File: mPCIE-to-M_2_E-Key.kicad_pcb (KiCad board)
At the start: 2 copper layers, 10 parts, among them J2 Bus_M.2_Socket_E, Q1 BSS138K, Q2 BSS138K, U1 TL1963A

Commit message: updated files
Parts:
- added H1: M2.5, lib_fp:M2.5_MH, F.Cu at (145.9, 82.0)
- added H2: M2.5, lib_fp:M2.5_MH, F.Cu at (121.8, 82.0)
- added H3: M3.5, lib_fp:MountingHole_3.5mm_Pad_Via, F.Cu at (133.8, 84.2)
- added J1: Bus_PCI_Express_Mini, lib_fp:BUS_mPCIe, F.Cu at (130.0, 130.0)
- added R5: 100K, lib_fp:CRCW0603, F.Cu at (125.0, 121.8)
- C1: value 10uF -> 100nF; footprint lib_fp:CAPC160X80X88L35N -> lib_fp:MLCC0603
- C2: value 10uF -> 470nF; footprint lib_fp:CAPC160X80X88L35N -> lib_fp:MLCC0805
- R1, R2, R3, R4: footprint lib_fp:RESC160X80X55L30N -> lib_fp:CRCW0603
- U1: value TL1963A -> TPS79718; footprint lib_fp:SOT223-4 -> lib_fp:SOT323-65P210X110-5
- moved C1 43.0 mm to (120.4, 122.8), turned to 90 degrees
- moved C2 35.9 mm to (126.8, 121.7), turned to 90 degrees
- moved Q1 30.2 mm to (129.5, 122.3), turned to 180 degrees
- moved U1 29.2 mm to (122.9, 122.8), turned to 180 degrees
- moved Q2 25.1 mm to (133.1, 122.3), turned to 180 degrees
- moved J2 21.2 mm to (133.8, 112.5), turned to 180 degrees
- moved R1 16.0 mm to (137.2, 123.4), turned to 90 degrees
- moved R3 15.1 mm to (129.5, 119.8), turned to 180 degrees
- moved R2 14.4 mm to (135.8, 123.4), turned to 90 degrees
- moved R4 8.31 mm to (136.5, 120.9)
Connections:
- net Net-(Q1-Pad3) renamed /SCL_3V3
- net Net-(Q2-Pad3) renamed /SDA_3V3
- J2 pad S1: Net-(J2-PadS1) -> GND
- J2 pad S2: Net-(J2-PadS1) -> GND
- Q1 pad 2: Net-(Q1-Pad2) -> /SCL_1V8
- Q2 pad 2: Net-(Q2-Pad2) -> /SDA_1V8
- R3 pad 2: Net-(Q1-Pad2) -> /SCL_1V8
- R4 pad 2: Net-(Q2-Pad2) -> /SDA_1V8
- U1 pad 1: +3V3 -> Net-(U1-PG)
- U1 pad 3: +1V8 -> unconnected-(U1-NC-Pad3)
- U1 pad 4: GND -> +3V3
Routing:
- net +3V3: track 0.00 -> 101.5 mm, vias 0 -> 3
- net GND: track 0.00 -> 66.2 mm, vias 0 -> 77
- net /W_DISABLE: track 0.00 -> 43.7 mm, vias 0 -> 3
- net /SCL_1V8: track 0.00 -> 22.8 mm
- net /SDA_1V8: track 0.00 -> 21.3 mm
- net /SCL_3V3: track 0.00 -> 17.3 mm, vias 0 -> 1
- net +1V8: track 0.00 -> 16.0 mm
- net /D_P: track 0.00 -> 12.2 mm, vias 0 -> 1
- net /D_N: track 0.00 -> 12.1 mm, vias 0 -> 1
- net /SDA_3V3: track 0.00 -> 11.2 mm, vias 0 -> 1
- net Net-(U1-PG): track 0.00 -> 1.68 mm
- added copper zone on B.Cu, net GND
- added copper zone on F.Cu, net GND
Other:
- board outline added: 30 x 47 mm

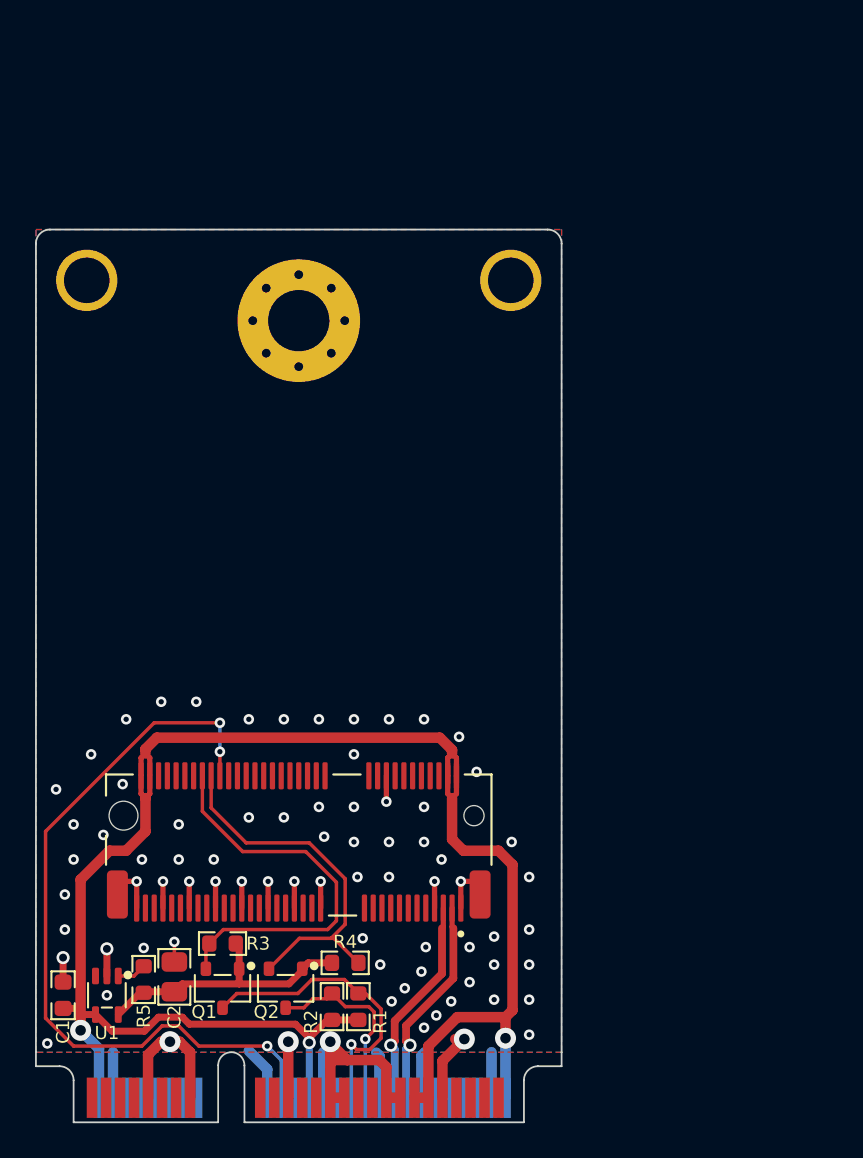
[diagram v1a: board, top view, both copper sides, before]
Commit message: added level shift and breakout for UART/I2C
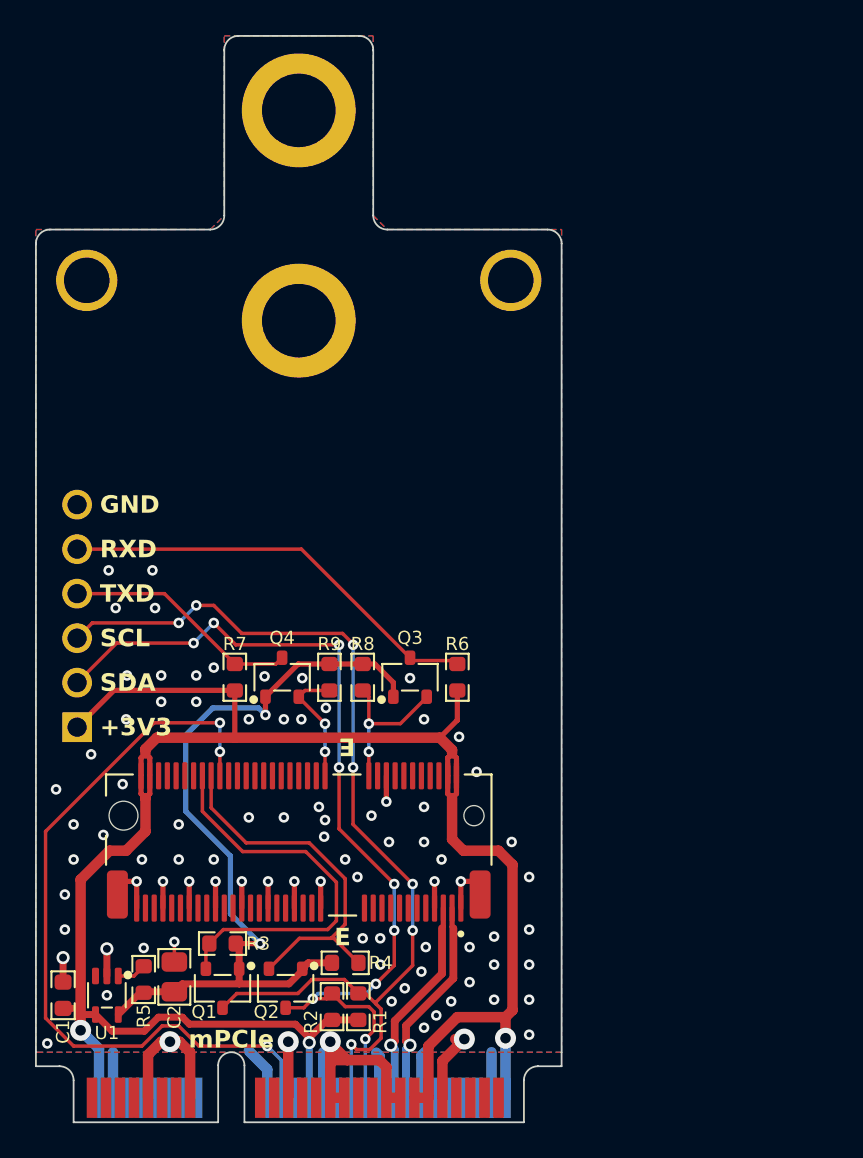
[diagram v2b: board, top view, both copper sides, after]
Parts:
- added H4: M3.5, lib_fp:MountingHole_3.5mm_Pad_Via, F.Cu at (133.8, 72.2)
- added J3: Conn_01x06_Pin, DS-Rectangular-Connectors:conn_01x06_254, F.Cu at (121.2, 101.1)
- added Q3: BSS138K, lib_fp:SOT23-3P95_237X112L50X40N, F.Cu at (140.2, 104.6)
- added Q4: BSS138K, lib_fp:SOT23-3P95_237X112L50X40N, F.Cu at (132.9, 104.6)
- added R6: 4K7, lib_fp:CRCW0603, F.Cu at (142.9, 104.6)
- added R7: 4K7, lib_fp:CRCW0603, F.Cu at (130.2, 104.6)
- added R8: 4K7, lib_fp:CRCW0603, F.Cu at (137.5, 104.6)
- added R9: 4K7, lib_fp:CRCW0603, F.Cu at (135.6, 104.6)
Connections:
- J2 pad 22: unconnected-(J2-UART_RXD-Pad22) -> /RXD_1V8
- J2 pad 32: unconnected-(J2-UART_TXD-Pad32) -> /TXD_1V8
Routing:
- net /SDA_3V3: track 11.2 -> 53.1 mm, vias 1 -> 9
- net /SCL_3V3: track 17.3 -> 57.9 mm, vias 1 -> 7
- net +1V8: track 16.0 -> 46.7 mm, vias 0 -> 2
- net /RXD_3V3: track 0.00 -> 24.4 mm
- net +3V3: track 101.5 -> 117.2 mm
- net /TXD_3V3: track 0.00 -> 13.5 mm
- net /RXD_1V8: track 0.00 -> 8.97 mm, vias 0 -> 2
- net /TXD_1V8: track 0.00 -> 7.03 mm, vias 0 -> 2
- net GND: vias 77 -> 87
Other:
- board size 30 x 47 mm -> 30 x 58 mm
- board text added: "+3V3"
- board text added: "E"
- board text added: "GND"
- board text added: "M.2 E-Key to mPCIe Adapter"
- board text added: "RXD"
- board text added: "SCL"
- board text added: "SDA"
- board text added: "TXD"
- board text added: "mPCIe"
